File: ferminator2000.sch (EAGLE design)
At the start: 120 parts, among them CN1 MINIB, IC1 FT232RL, IC2 REF01D, Q1 STP5NA50, Q2 STP5NA50, SW1 ENCODER_SW1-PEC12, U1 DSPIC33FJ256GP510A

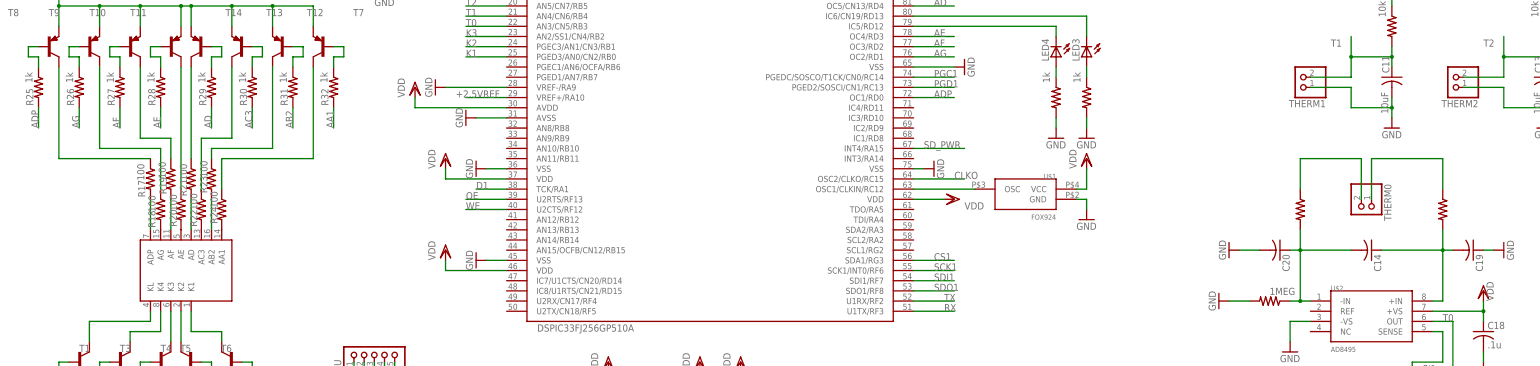
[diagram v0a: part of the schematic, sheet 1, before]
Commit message: added pin definitions
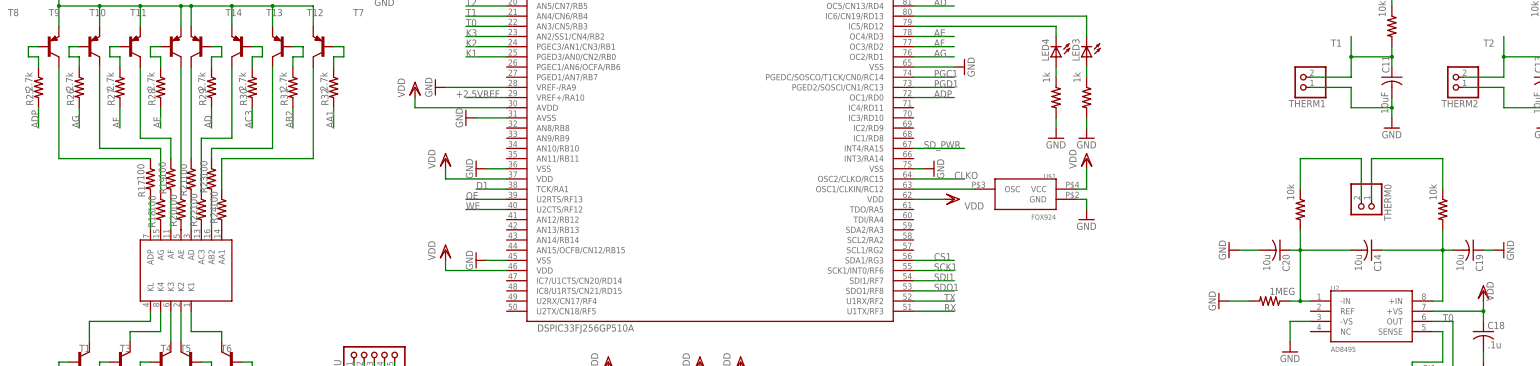
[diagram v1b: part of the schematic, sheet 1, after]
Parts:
- C1: value (none) -> 100u
- C14, C19, C20: value (none) -> 10u
- R10, R11, R12, R13, R8, R9: value 47k -> 10k
- R16: value 1k -> 22
- R2, R3: value 1K -> 1k
- R25, R26, R27, R28, R29, R30, R31, R32: value 1k -> 2.7k
- R4, R6: value 1k -> 5.6k
- R41, R42: value (none) -> 10k
- renumbered U$2 to U2
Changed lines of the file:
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@@
 <part name="VDD20" library="supply1" deviceset="VDD" device=""/>
 <part name="GND34" library="supply1" deviceset="GND" device=""/>
-<part name="U$2" library="eric_sorensen" deviceset="AD8497" device="" value="AD8495"/>
+<part name="U2" library="eric_sorensen" deviceset="AD8497" device="" value="AD8495"/>
 <part name="GND1" library="supply1" deviceset="GND" device=""/>
-<part name="R8" library="rcl" deviceset="R-US_" device="R0805" value="47k"/>
-<part name="R9" library="rcl" deviceset="R-US_" device="R0805" value="47k"/>
-<part name="R10" library="rcl" deviceset="R-US_" device="R0805" value="47k"/>
-<part name="R11" library="rcl" deviceset="R-US_" device="R0805" value="47k"/>
-<part name="R12" library="rcl" deviceset="R-US_" device="R0805" value="47k"/>
-<part name="R13" library="rcl" deviceset="R-US_" device="R0805" value="47k"/>
+<part name="R8" library="rcl" deviceset="R-US_" device="R0805" value="10k"/>
+<part name="R9" library="rcl" deviceset="R-US_" device="R0805" value="10k"/>
+<part name="R10" library="rcl" deviceset="R-US_" device="R0805" value="10k"/>
+<part name="R11" library="rcl" deviceset="R-US_" device="R0805" value="10k"/>
+<part name="R12" library="rcl" deviceset="R-US_" device="R0805" value="10k"/>
+<part name="R13" library="rcl" deviceset="R-US_" device="R0805" value="10k"/>
 <part name="VDD1" library="supply1" deviceset="VDD" device=""/>
 <part name="VDD2" library="supply1" deviceset="VDD" device=""/>
 <part name="CONN2" library="main2" deviceset="NEARLAB_SDCARD_HOLDER" device=""/>
 <part name="T2" library="zetex" deviceset="NMOSSOT23" device=""/>
-<part name="R16" library="rcl" deviceset="R-US_" device="R0805" value="1k"/>
+<part name="R16" library="rcl" deviceset="R-US_" device="R0805" value="22"/>
 <part name="R1" library="rcl" deviceset="R-US_" device="R0805" value="470"/>
 <part name="C4" library="rcl" deviceset="C-US" device="C0603" value=".1u"/>
@@
 <part name="TX" library="adafruit" deviceset="LED" device="CHIP-LED0805" value="Red"/>
 <part name="RX" library="adafruit" deviceset="LED" device="CHIP-LED0805" value="Green"/>
-<part name="R2" library="adafruit" deviceset="R-US_" device="R0805" value="1K"/>
-<part name="R3" library="adafruit" deviceset="R-US_" device="R0805" value="1K"/>
+<part name="R2" library="adafruit" deviceset="R-US_" device="R0805" value="1k"/>
+<part name="R3" library="adafruit" deviceset="R-US_" device="R0805" value="1k"/>
 <part name="R5" library="adafruit" deviceset="R-US_" device="R0805" value="10"/>
 <part name="P+1" library="supply1" deviceset="+5V" device=""/>
@@
 <part name="C9" library="rcl" deviceset="C-US" device="C0603" value=".1u"/>
 <part name="LED7" library="adafruit" deviceset="LED" device="CHIP-LED0805" value="Red"/>
-<part name="R4" library="rcl" deviceset="R-US_" device="R0805" value="1k"/>
+<part name="R4" library="rcl" deviceset="R-US_" device="R0805" value="5.6k"/>
 <part name="LED8" library="adafruit" deviceset="LED" device="CHIP-LED0805" value="Red"/>
-<part name="R6" library="rcl" deviceset="R-US_" device="R0805" value="1k"/>
+<part name="R6" library="rcl" deviceset="R-US_" device="R0805" value="5.6k"/>
 <part name="U$3" library="eric_sorensen" deviceset="PHOENIX-3.5MM" device=""/>
 <part name="P+6" library="supply1" deviceset="+24V" device=""/>
@@
 <part name="R23" library="rcl" deviceset="R-US_" device="R0805" value="100"/>
 <part name="R24" library="rcl" deviceset="R-US_" device="R0805" value="100"/>
-<part name="R25" library="rcl" deviceset="R-US_" device="R0805" value="1k"/>
-<part name="R26" library="rcl" deviceset="R-US_" device="R0805" value="1k"/>
-<part name="R27" library="rcl" deviceset="R-US_" device="R0805" value="1k"/>
-<part name="R28" library="rcl" deviceset="R-US_" device="R0805" value="1k"/>
-<part name="R29" library="rcl" deviceset="R-US_" device="R0805" value="1k"/>
-<part name="R30" library="rcl" deviceset="R-US_" device="R0805" value="1k"/>
-<part name="R31" library="rcl" deviceset="R-US_" device="R0805" value="1k"/>
-<part name="R32" library="rcl" deviceset="R-US_" device="R0805" value="1k"/>
+<part name="R25" library="rcl" deviceset="R-US_" device="R0805" value="2.7k"/>
+<part name="R26" library="rcl" deviceset="R-US_" device="R0805" value="2.7k"/>
+<part name="R27" library="rcl" deviceset="R-US_" device="R0805" value="2.7k"/>
+<part name="R28" library="rcl" deviceset="R-US_" device="R0805" value="2.7k"/>
+<part name="R29" library="rcl" deviceset="R-US_" device="R0805" value="2.7k"/>
+<part name="R30" library="rcl" deviceset="R-US_" device="R0805" value="2.7k"/>
+<part name="R31" library="rcl" deviceset="R-US_" device="R0805" value="2.7k"/>
+<part name="R32" library="rcl" deviceset="R-US_" device="R0805" value="2.7k"/>
 <part name="R33" library="rcl" deviceset="R-US_" device="R0805" value="1k"/>
 <part name="R34" library="rcl" deviceset="R-US_" device="R0805" value="1k"/>
@@
 <part name="R40" library="rcl" deviceset="R-US_" device="R0805" value="1MEG"/>
 <part name="GND26" library="supply1" deviceset="GND" device=""/>
-<part name="C14" library="rcl" deviceset="C-US" device="C0603"/>
-<part name="C19" library="rcl" deviceset="C-US" device="C0603"/>
-<part name="C20" library="rcl" deviceset="C-US" device="C0603"/>
+<part name="C14" library="rcl" deviceset="C-US" device="C0603" value="10u"/>
+<part name="C19" library="rcl" deviceset="C-US" device="C0603" value="10u"/>
+<part name="C20" library="rcl" deviceset="C-US" device="C0603" value="10u"/>
 <part name="GND27" library="supply1" deviceset="GND" device=""/>
 <part name="GND28" library="supply1" deviceset="GND" device=""/>
-<part name="R41" library="rcl" deviceset="R-US_" device="R0805"/>
-<part name="R42" library="rcl" deviceset="R-US_" device="R0805"/>
+<part name="R41" library="rcl" deviceset="R-US_" device="R0805" value="10k"/>
+<part name="R42" library="rcl" deviceset="R-US_" device="R0805" value="10k"/>
 <part name="THERM0" library="pinhead" deviceset="PINHD-1X2" device=""/>
 <part name="GND31" library="supply1" deviceset="GND" device=""/>
@@
 <part name="GND3" library="supply1" deviceset="GND" device=""/>
 <part name="D1" library="diode" deviceset="DIODE-" device="SOD323-R"/>
-<part name="C1" library="rcl" deviceset="CPOL-EU" device="UD-6,3X8,8"/>
+<part name="C1" library="rcl" deviceset="CPOL-EU" device="UD-6,3X8,8" value="100u"/>
 <part name="CPU" library="pinhead" deviceset="PINHD-1X5" device=""/>
 <part name="GND4" library="supply1" deviceset="GND" device=""/>
@@
 <instance part="VDD20" gate="G$1" x="416.56" y="40.64"/>
 <instance part="GND34" gate="1" x="416.56" y="17.78"/>
-<instance part="U$2" gate="G$1" x="574.04" y="50.8"/>
+<instance part="U2" gate="G$1" x="574.04" y="50.8"/>
 <instance part="R1" gate="G$1" x="335.28" y="147.32" rot="R180"/>
 <instance part="C4" gate="G$1" x="327.66" y="142.24"/>
@@
 </segment>
 <segment>
-<pinref part="U$2" gate="G$1" pin="+VS"/>
+<pinref part="U2" gate="G$1" pin="+VS"/>
 <wire x1="589.28" y1="53.34" x2="601.98" y2="53.34" width="0.1524" layer="91"/>
 <wire x1="601.98" y1="53.34" x2="601.98" y2="55.88" width="0.1524" layer="91"/>
@@
 <pinref part="GND31" gate="1" pin="GND"/>
 <wire x1="553.72" y1="45.72" x2="553.72" y2="50.8" width="0.1524" layer="91"/>
-<pinref part="U$2" gate="G$1" pin="-VS"/>
+<pinref part="U2" gate="G$1" pin="-VS"/>
 <wire x1="553.72" y1="50.8" x2="558.8" y2="50.8" width="0.1524" layer="91"/>
 </segment>
@@
 </segment>
 <segment>
-<pinref part="U$2" gate="G$1" pin="OUT"/>
+<pinref part="U2" gate="G$1" pin="OUT"/>
 <wire x1="589.28" y1="50.8" x2="594.36" y2="50.8" width="0.1524" layer="91"/>
 <label x="591.82" y="50.8" size="1.778" layer="95"/>
@@
 <segment>
 <pinref part="R40" gate="G$1" pin="1"/>
-<pinref part="U$2" gate="G$1" pin="-IN"/>
+<pinref part="U2" gate="G$1" pin="-IN"/>
 <wire x1="553.72" y1="55.88" x2="556.26" y2="55.88" width="0.1524" layer="91"/>
 <wire x1="556.26" y1="55.88" x2="558.8" y2="55.88" width="0.1524" layer="91"/>
@@
 <wire x1="591.82" y1="68.58" x2="591.82" y2="55.88" width="0.1524" layer="91"/>
 <junction x="591.82" y="68.58"/>
-<pinref part="U$2" gate="G$1" pin="+IN"/>
+<pinref part="U2" gate="G$1" pin="+IN"/>
 <wire x1="591.82" y1="55.88" x2="589.28" y2="55.88" width="0.1524" layer="91"/>
 <pinref part="R42" gate="G$1" pin="2"/>
@@
 <wire x1="584.2" y1="40.64" x2="591.82" y2="40.64" width="0.1524" layer="91"/>
 <wire x1="591.82" y1="40.64" x2="591.82" y2="48.26" width="0.1524" layer="91"/>
-<pinref part="U$2" gate="G$1" pin="SENSE"/>
+<pinref part="U2" gate="G$1" pin="SENSE"/>
 <wire x1="591.82" y1="48.26" x2="589.28" y2="48.26" width="0.1524" layer="91"/>
 </segment>

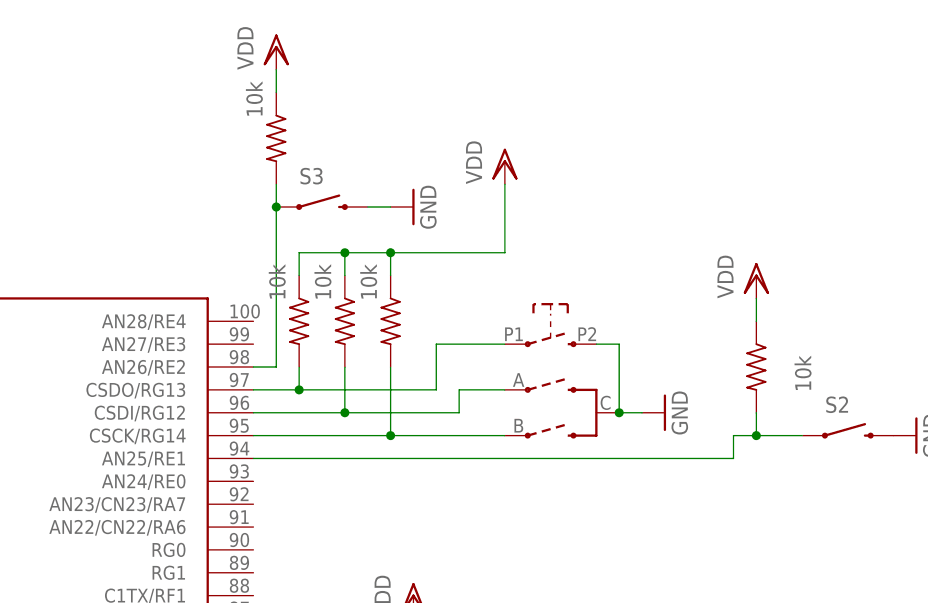
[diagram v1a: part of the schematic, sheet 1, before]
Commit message: Added Control Lines for FETs
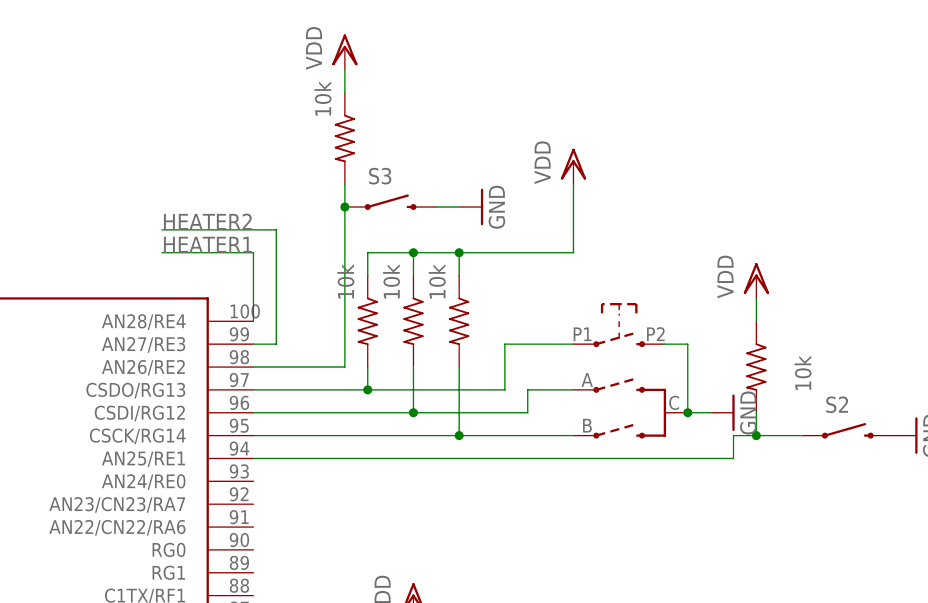
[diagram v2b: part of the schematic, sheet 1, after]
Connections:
- net HEATER1: now also U1.AN28/RE4
- net HEATER2: now also U1.AN27/RE3
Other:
- moved on the sheet: S3
